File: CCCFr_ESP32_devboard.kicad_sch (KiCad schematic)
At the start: 75 parts, among them J1 USB_C_Receptacle_USB2.0_14P, J2 Conn_01x02_Pin, J3 Conn_01x18_Pin, J5 Conn_01x18_Pin, Q1 AO3401A, U1 ESP32-S3, U2 W25Q128JVS, U3 MCP73831-2-OT, U4 AMS1117-3.3, Y1 32.768 kHz, Y2 40MHz(10ppm)

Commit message: integrated bottle opener
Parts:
- removed BTN1: BTN, Button_Switch_SMD:SW_Push_1P1T_XKB_TS-1187A, symbol Switch:SW_Push
- removed R4: 10K, Resistor_SMD:R_0402_1005Metric, symbol Device:R
- added BTN2, BTN3, BTN4, BTN5, BTN6, BTN7: BTN, Button_Switch_SMD:SW_Push_1P1T_XKB_TS-1187A, symbol Switch:SW_Push
- added R3, R5, R6, R7, R8, R9: 10K, Resistor_SMD:R_0402_1005Metric, symbol Device:R
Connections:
- net +3V3: now also R3.1, R5.1, R6.1, R7.1, R8.1, R9.1
- net GND: now also BTN2.1, BTN3.1, BTN4.1, BTN5.1, BTN6.1, BTN7.1
- net IO34: now also BTN2.2, R3.2; no longer J5.16 (Pin_16)
- net IO35: now also BTN3.2, R5.2; no longer J5.15 (Pin_15)
- net IO36: now also BTN4.2, R6.2; no longer J5.13 (Pin_13)
- net IO37: now also BTN5.2, R7.2; no longer J5.11 (Pin_11)
- net IO38: now also BTN6.2, R8.2; no longer J5.5 (Pin_5)
- net IO39: now also BTN7.2, R9.2; no longer J5.4 (Pin_4)
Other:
- note added: "FLASH MEMORY"
- note added: "For blinking LED test: GPIO01"
- note added: "power on LED"
- note removed: "EXTRA MEMORY"

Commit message: Added 60 pieces of 2812B in the shape of CCCFr
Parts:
- added C1, C12, C21, C23, C24, C27, C28, C29, C30, C34, C41, C42, C43, C44, C45, C46, C47, C48, C49, C5, C50, C51, C52, C53, C54, C55, C56, C57, C58, C59, C60, C61, C62, C63, C64, C65, C66, C67, C68, C69, C70, C71, C72, C73, C74, C75, C76, C77, C78, C79, C80, C81, C82, C83, C84, C85, C86, C87, C88, C9: 0.1uF, Capacitor_SMD:C_0402_1005Metric, symbol Device:C
- added D10, D11, D12, D13, D14, D15, D16, D17, D18, D19, D20, D21, D22, D23, D24, D25, D26, D27, D28, D29, D30, D31, D32, D33, D34, D35, D36, D37, D38, D39, D40, D41, D42, D43, D44, D45, D46, D47, D48, D49, D5, D50, D51, D52, D53, D54, D55, D56, D57, D58, D59, D6, D60, D61, D62, D63, D64, D7, D8, D9: XL-1615RGBC-2812B, kustom:XL-1615RGBC-2812B, symbol kustom:XL-1615RGBC-2812B
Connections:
- net GND: now also C1.2, C12.2, C21.2, C23.2, C24.2, C27.2, C28.2, C29.2, C30.2, C34.2, C41.2, C42.2, C43.2, C44.2, C45.2, C46.2, C47.2, C48.2, C49.2, C5.2, C50.2, C51.2, C52.2, C53.2, C54.2, C55.2, C56.2, C57.2, C58.2, C59.2, C60.2, C61.2, C62.2, C63.2, C64.2, C65.2, C66.2, C67.2, C68.2, C69.2, C70.2, C71.2, C72.2, C73.2, C74.2, C75.2, C76.2, C77.2, C78.2, C79.2, C80.2, C81.2, C82.2, C83.2, C84.2, C85.2, C86.2, C87.2, C88.2, C9.2, D10.1 (GND), D11.1 (GND), D12.1 (GND), D13.1 (GND), D14.1 (GND), D15.1 (GND), D16.1 (GND), D17.1 (GND), D18.1 (GND), D19.1 (GND), D20.1 (GND), D21.1 (GND), D22.1 (GND), D23.1 (GND), D24.1 (GND), D25.1 (GND), D26.1 (GND), D27.1 (GND), D28.1 (GND), D29.1 (GND), D30.1 (GND), D31.1 (GND), D32.1 (GND), D33.1 (GND), D34.1 (GND), D35.1 (GND), D36.1 (GND), D37.1 (GND), D38.1 (GND), D39.1 (GND), D40.1 (GND), D41.1 (GND), D42.1 (GND), D43.1 (GND), D44.1 (GND), D45.1 (GND), D46.1 (GND), D47.1 (GND), D48.1 (GND), D49.1 (GND), D5.1 (GND), D50.1 (GND), D51.1 (GND), D52.1 (GND), D53.1 (GND), D54.1 (GND), D55.1 (GND), D56.1 (GND), D57.1 (GND), D58.1 (GND), D59.1 (GND), D6.1 (GND), D60.1 (GND), D61.1 (GND), D62.1 (GND), D63.1 (GND), D64.1 (GND), D7.1 (GND), D8.1 (GND), D9.1 (GND)
- new net: D49.4 (DOUT), D50.2 (DIN)
- new net: C74.1, D50.3 (VDD)
- new net: D50.4 (DOUT), D51.2 (DIN)
- new net: C84.1, D61.3 (VDD)
- new net: D54.4 (DOUT), D55.2 (DIN)
- new net: C78.1, D55.3 (VDD)
- new net: D55.4 (DOUT), D56.2 (DIN)
- new net: C65.1, D41.3 (VDD)
- new net: D62.4 (DOUT), D63.2 (DIN)
- new net: C86.1, D63.3 (VDD)
- new net: D63.4 (DOUT), D64.2 (DIN)
- new net: C73.1, D49.3 (VDD)
- new net: C45.1, D21.3 (VDD)
- new net: D16.4 (DOUT), D17.2 (DIN)
- new net: C41.1, D17.3 (VDD)
- new net: D17.4 (DOUT), D18.2 (DIN)
- new net: D32.4 (DOUT), D33.2 (DIN)
- new net: C57.1, D33.3 (VDD)
- new net: D33.4 (DOUT), D34.2 (DIN)
- new net: C82.1, D59.3 (VDD)
- new net: D61.4 (DOUT), D62.2 (DIN)
- new net: C85.1, D62.3 (VDD)
- new net: C30.1, D15.3 (VDD)
- new net: C63.1, D39.3 (VDD)
- new net: C62.1, D38.3 (VDD)
- new net: D10.2 (DIN), D9.4 (DOUT)
- new net: C23.1, D10.3 (VDD)
- new net: D10.4 (DOUT), D11.2 (DIN)
- new net: D57.4 (DOUT), D58.2 (DIN)
- new net: C81.1, D58.3 (VDD)
- new net: D58.4 (DOUT), D59.2 (DIN)
- new net: C69.1, D45.3 (VDD)
- new net: C87.1, D64.3 (VDD)
- new net: D30.4 (DOUT), D31.2 (DIN)
- new net: C55.1, D31.3 (VDD)
- new net: D31.4 (DOUT), D32.2 (DIN)
- new net: C42.1, D18.3 (VDD)
- new net: D18.4 (DOUT), D19.2 (DIN)
- new net: C53.1, D29.3 (VDD)
- new net: D36.4 (DOUT), D37.2 (DIN)
- new net: C61.1, D37.3 (VDD)
- new net: D37.4 (DOUT), D38.2 (DIN)
- new net: D19.4 (DOUT), D20.2 (DIN)
- new net: C44.1, D20.3 (VDD)
- new net: D20.4 (DOUT), D21.2 (DIN)
- new net: C24.1, D11.3 (VDD)
- new net: D11.4 (DOUT), D12.2 (DIN)
- new net: C68.1, D44.3 (VDD)
- new net: D13.4 (DOUT), D14.2 (DIN)
- new net: C29.1, D14.3 (VDD)
- new net: D14.4 (DOUT), D15.2 (DIN)
- new net: C27.1, D12.3 (VDD)
- new net: D12.4 (DOUT), D13.2 (DIN)
- new net: D59.4 (DOUT), D60.2 (DIN)
- new net: C83.1, D60.3 (VDD)
- new net: D60.4 (DOUT), D61.2 (DIN)
- new net: C75.1, D51.3 (VDD)
- new net: C72.1, D48.3 (VDD)
- new net: D38.4 (DOUT), D39.2 (DIN)
- new net: D39.4 (DOUT), D40.2 (DIN)
- new net: D8.4 (DOUT), D9.2 (DIN)
- new net: C21.1, D9.3 (VDD)
- new net: C54.1, D30.3 (VDD)
- new net: C1.1, D5.3 (VDD)
- new net: D5.4 (DOUT), D6.2 (DIN)
- new net: C47.1, D23.3 (VDD)
- new net: D27.4 (DOUT), D28.2 (DIN)
- new net: C52.1, D28.3 (VDD)
- new net: D28.4 (DOUT), D29.2 (DIN)
- new net: C58.1, D34.3 (VDD)
- new net: D24.4 (DOUT), D25.2 (DIN)
- new net: C49.1, D25.3 (VDD)
- new net: D25.4 (DOUT), D26.2 (DIN)
- new net: C46.1, D22.3 (VDD)
- new net: D46.4 (DOUT), D47.2 (DIN)
- new net: C71.1, D47.3 (VDD)
- new net: D47.4 (DOUT), D48.2 (DIN)
- new net: C5.1, D6.3 (VDD)
- new net: D6.4 (DOUT), D7.2 (DIN)
- new net: C9.1, D7.3 (VDD)
- new net: C59.1, D35.3 (VDD)
- new net: D51.4 (DOUT), D52.2 (DIN)
- new net: C60.1, D36.3 (VDD)
- new net: D7.4 (DOUT), D8.2 (DIN)
- new net: C70.1, D46.3 (VDD)
- new net: D22.4 (DOUT), D23.2 (DIN)
- new net: D23.4 (DOUT), D24.2 (DIN)
- new net: D34.4 (DOUT), D35.2 (DIN)
- new net: D44.4 (DOUT), D45.2 (DIN)
- new net: D45.4 (DOUT), D46.2 (DIN)
- new net: D21.4 (DOUT), D22.2 (DIN)
- new net: D52.4 (DOUT), D53.2 (DIN)
- new net: C88.1, D53.3 (VDD)
- new net: D53.4 (DOUT), D54.2 (DIN)
- new net: C51.1, D27.3 (VDD)
- new net: D15.4 (DOUT), D16.2 (DIN)
- new net: D41.4 (DOUT), D42.2 (DIN)
- new net: C66.1, D42.3 (VDD)
- new net: D42.4 (DOUT), D43.2 (DIN)
- new net: C76.1, D52.3 (VDD)
- new net: D43.4 (DOUT), D44.2 (DIN)
- new net: C79.1, D56.3 (VDD)
- new net: D56.4 (DOUT), D57.2 (DIN)
- new net: C48.1, D24.3 (VDD)
- new net: C56.1, D32.3 (VDD)
- new net: D48.4 (DOUT), D49.2 (DIN)
- new net: C50.1, D26.3 (VDD)
- new net: D26.4 (DOUT), D27.2 (DIN)
- new net: C67.1, D43.3 (VDD)
- new net: D29.4 (DOUT), D30.2 (DIN)
- new net: C77.1, D54.3 (VDD)
- new net: C34.1, D16.3 (VDD)
- new net: D35.4 (DOUT), D36.2 (DIN)
- new net: C28.1, D13.3 (VDD)
- new net: C80.1, D57.3 (VDD)
- new net: C12.1, D8.3 (VDD)
- new net: C43.1, D19.3 (VDD)
- new net: C64.1, D40.3 (VDD)
- new net: D40.4 (DOUT), D41.2 (DIN)
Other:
- note added: "LEDs"
- note removed: "LEDs/BILDSCHIRM"

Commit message: Added buttons
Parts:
- added C89, C90, C91, C92, C93: 10uF, Capacitor_SMD:C_0402_1005Metric, symbol Device:C
- added L1: 1uH, Inductor_SMD:L_TechFuse_SL0420, symbol Device:L
- added R10: 732K, Resistor_SMD:R_1206_3216Metric, symbol Device:R
- added R4: 100K, Resistor_SMD:R_0402_1005Metric, symbol Device:R
- added U5: TPS61023DRLR, PCM_SparkFun-Semiconductor-Standard:SOT-563, symbol kustom:TPS61023DRLR
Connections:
- net GND: now also C89.2, C90.2, C91.2, C92.2, C93.2, R4.2, U5.4 (GND)
- net IO21: now also D5.2 (DIN); no longer J3.14 (Pin_14)
- net IO5: now also U5.2 (EN); no longer J3.6 (Pin_6)
- net VSYS: now also C89.1, L1.1, U5.3 (VIN)
- new net: R10.2, R4.1, U5.1 (FB)
- new net: L1.2, U5.5 (SW)
- new net LED_VDD: C90.1, C91.1, C92.1, C93.1, R10.1, U5.6 (VOUT)
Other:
- note added: "LED 5V"
- note added: "input only btn"
- note added: "input only?"
- note added: "logic high: enable"
- moved on the sheet: +3V3, AE1, BTN2, BTN3, BTN4, BTN5, BTN6, BTN7, C1, C10, C11, C12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

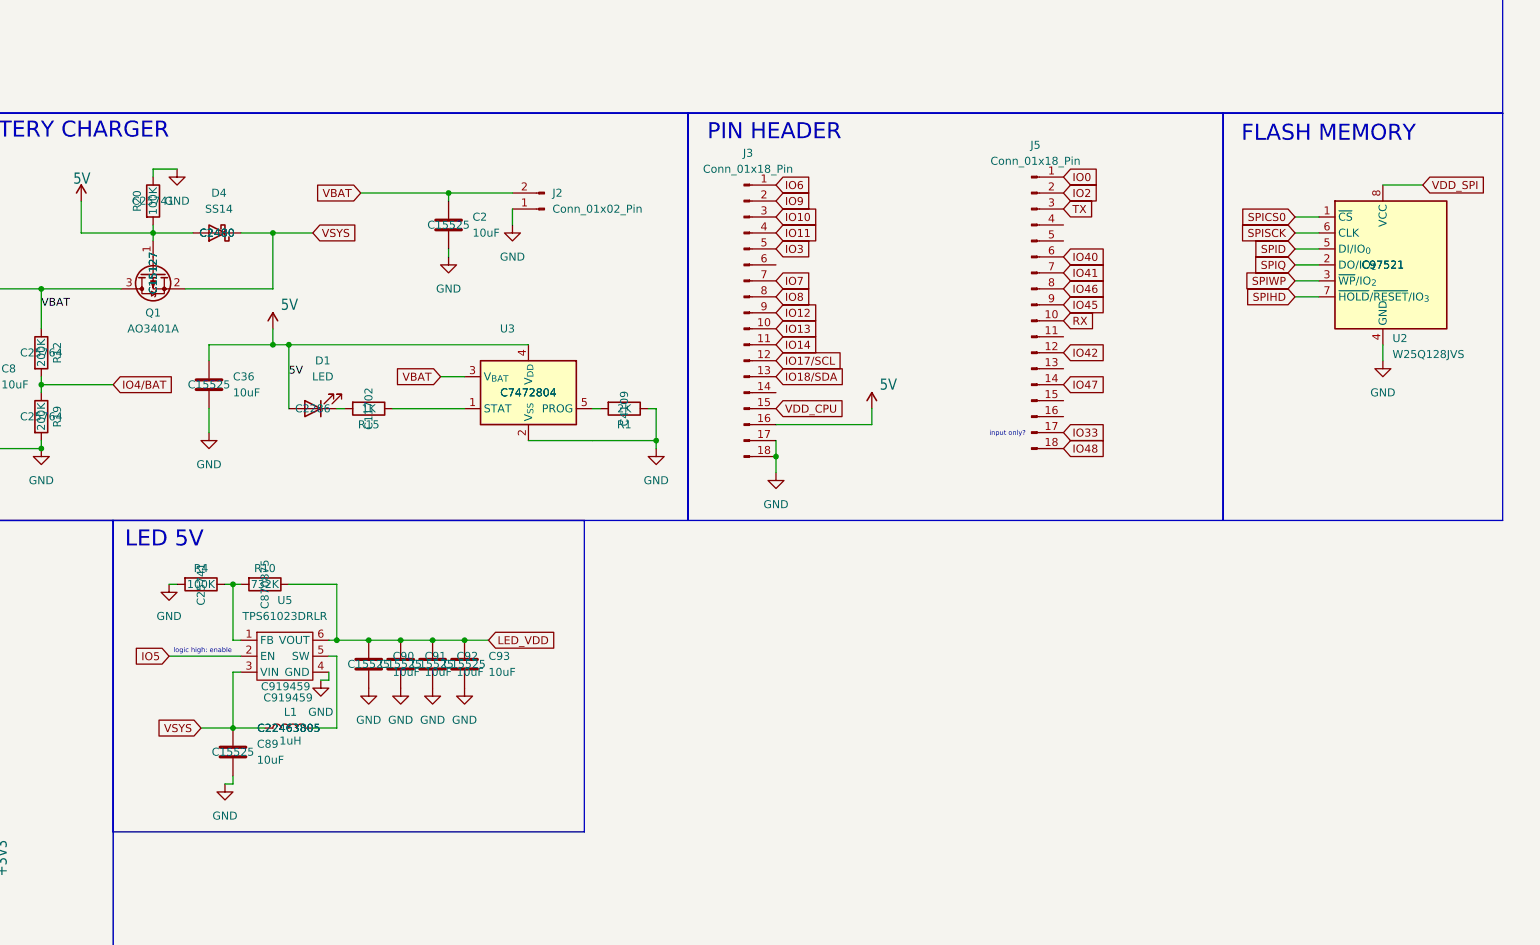
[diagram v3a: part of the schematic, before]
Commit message: rearrandged footprints
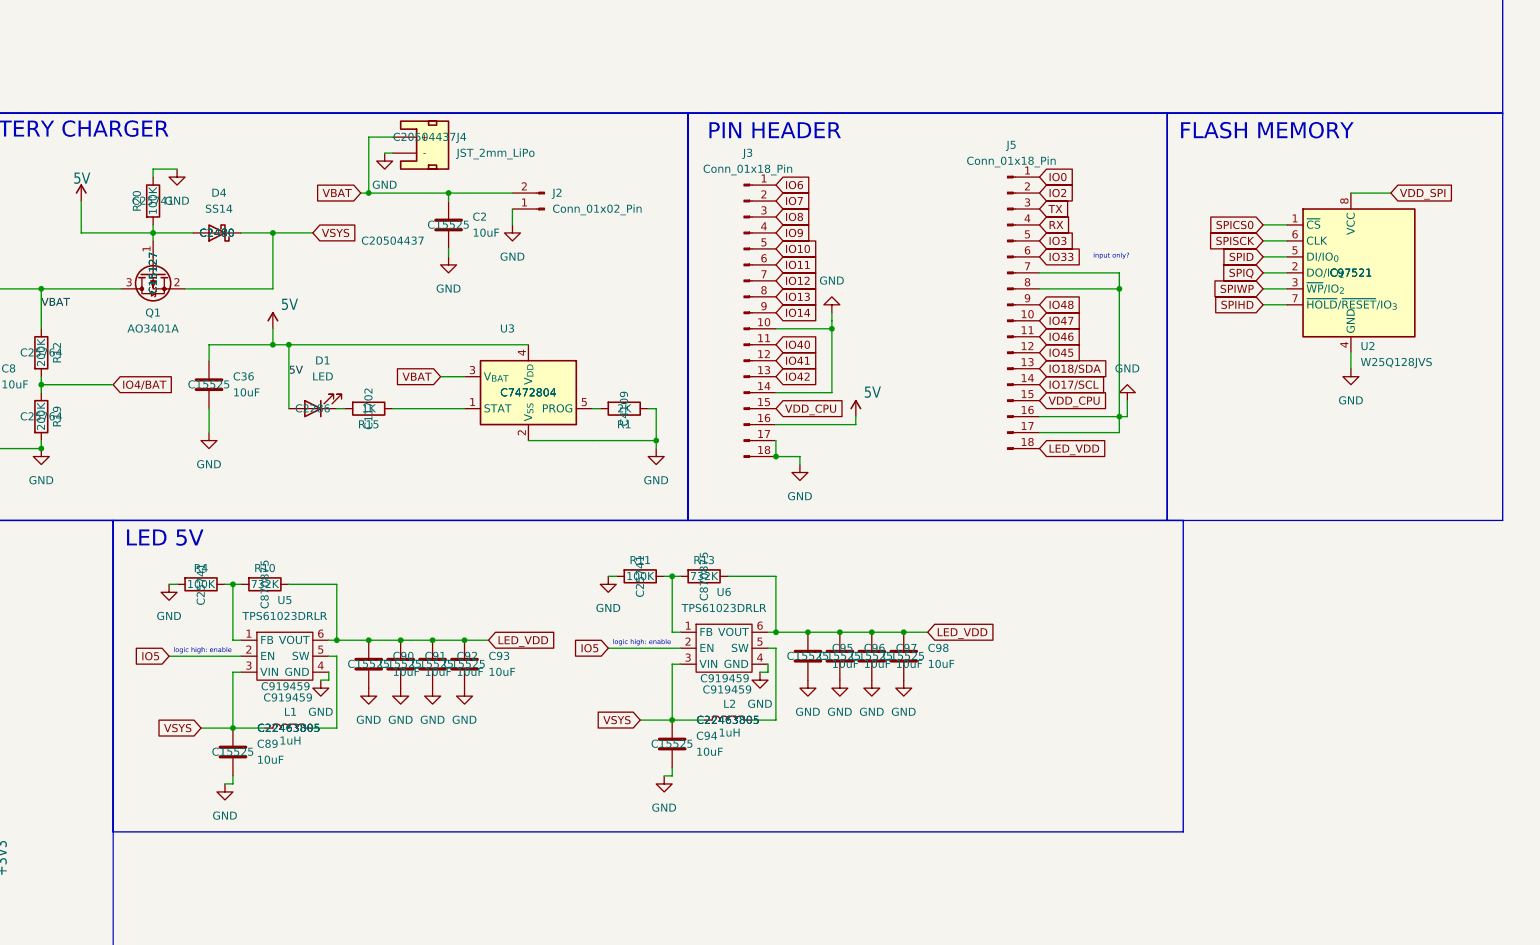
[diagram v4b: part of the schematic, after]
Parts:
- added C94, C95, C96, C97, C98: 10uF, Capacitor_SMD:C_0402_1005Metric, symbol Device:C
- added J4: JST_2mm_LiPo, PCM_SparkFun-Connector:JST_1x02_P2.0mm_Horizontal_SMD, symbol PCM_SparkFun-Connector:Conn_01x02_JST_P2.0mm_Horizontal_SMD_LiPo
- added L2: 1uH, Inductor_SMD:L_TechFuse_SL0420, symbol Device:L
- added R11: 100K, Resistor_SMD:R_0402_1005Metric, symbol Device:R
- added R13: 732K, Resistor_SMD:R_1206_3216Metric, symbol Device:R
- added U6: TPS61023DRLR, PCM_SparkFun-Semiconductor-Standard:SOT-563, symbol kustom:TPS61023DRLR
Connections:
- net +3V3: now also J5.15 (Pin_15)
- net GND: now also J3.10 (Pin_10), J3.14 (Pin_14), J5.16 (Pin_16), J5.17 (Pin_17), J5.7 (Pin_7), J5.8 (Pin_8), C94.2, C95.2, C96.2, C97.2, C98.2, J4.1 (-), R11.2, U6.4 (GND)
- net IO10: now also J3.5 (Pin_5); no longer J3.3 (Pin_3)
- net IO11: now also J3.6 (Pin_6); no longer J3.4 (Pin_4)
- net IO12: now also J3.7 (Pin_7); no longer J3.9 (Pin_9)
- net IO13: now also J3.8 (Pin_8); no longer J3.10 (Pin_10)
- net IO14: now also J3.9 (Pin_9); no longer J3.11 (Pin_11)
- net IO17/SCL: now also J5.14 (Pin_14); no longer J3.12 (Pin_12)
- net IO18/SDA: now also J5.13 (Pin_13); no longer J3.13 (Pin_13)
- net IO3: now also J5.5 (Pin_5); no longer J3.5 (Pin_5)
- net IO33: now also J5.6 (Pin_6); no longer J5.17 (Pin_17)
- net IO40: now also J3.11 (Pin_11); no longer J5.6 (Pin_6)
- net IO41: now also J3.12 (Pin_12); no longer J5.7 (Pin_7)
- net IO42: now also J3.13 (Pin_13); no longer J5.12 (Pin_12)
- net IO45: now also J5.12 (Pin_12); no longer J5.9 (Pin_9)
- net IO46: now also J5.11 (Pin_11); no longer J5.8 (Pin_8)
- net IO47: now also J5.10 (Pin_10); no longer J5.14 (Pin_14)
- net IO48: now also J5.9 (Pin_9); no longer J5.18 (Pin_18)
- net IO5: now also U6.2 (EN)
- net IO7: now also J3.2 (Pin_2); no longer J3.7 (Pin_7)
- net IO8: now also J3.3 (Pin_3); no longer J3.8 (Pin_8)
- net IO9: now also J3.4 (Pin_4); no longer J3.2 (Pin_2)
- net LED_VDD: now also J5.18 (Pin_18), C95.1, C96.1, C97.1, C98.1, R13.1, U6.6 (VOUT)
- net RX: now also J5.4 (Pin_4); no longer J5.10 (Pin_10)
- net VBAT: now also J4.2 (+)
- net VSYS: now also C94.1, L2.1, U6.3 (VIN)
- new net: L2.2, U6.5 (SW)
- new net: R11.1, R13.2, U6.1 (FB)
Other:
- moved on the sheet: J5, U2

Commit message: Added JST plug for battery
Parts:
- J4: footprint PCM_SparkFun-Connector:JST_1x02_P2.0mm_Horizontal_SMD -> Connector_JST:JST_PH_B2B-PH-K_1x02_P2.00mm_Vertical; PROD_ID (none) -> CONN-11443
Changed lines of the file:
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@@
 			)
 		)
-		(property "Footprint" "PCM_SparkFun-Connector:JST_1x02_P2.0mm_Horizontal_SMD"
+		(property "Footprint" "Connector_JST:JST_PH_B2B-PH-K_1x02_P2.00mm_Vertical"
 			(at 339.09 114.3 0)
 			(effects
@@
 			)
 		)
+		(property "PROD_ID" "CONN-11443"
+			(at 339.09 119.38 0)
+			(effects
+				(font
+					(size 1.27 1.27)
+				)
+				(hide yes)
+			)
+		)
